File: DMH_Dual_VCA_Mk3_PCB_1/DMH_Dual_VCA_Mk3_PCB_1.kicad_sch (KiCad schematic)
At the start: 0 parts

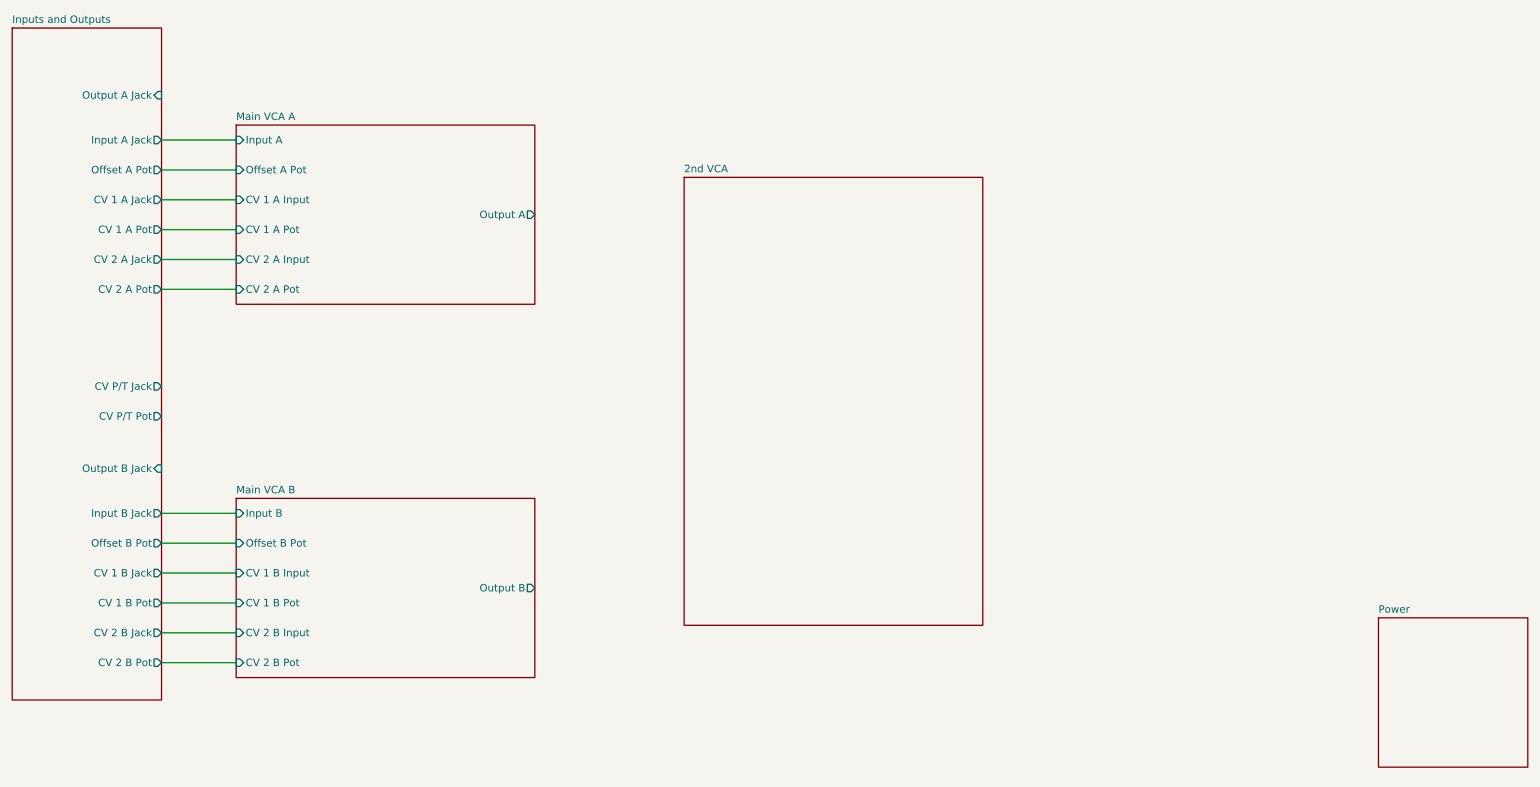
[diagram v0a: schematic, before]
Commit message: 2nd VCA design done
Clipping design in progress
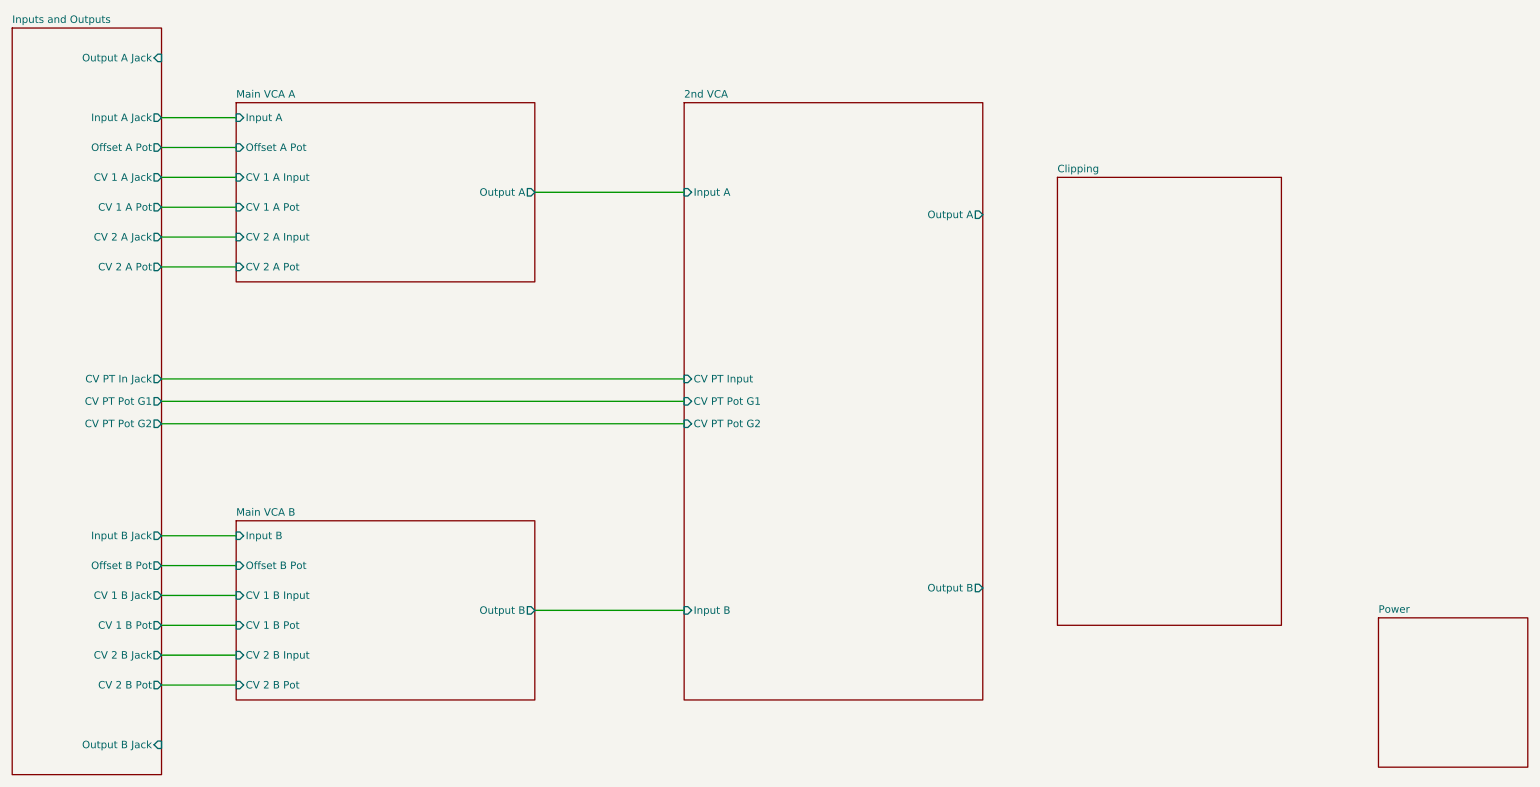
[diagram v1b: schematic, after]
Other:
- added sheet Clipping (Clipping.kicad_sch)
- sheet 2nd VCA ports: added CV PT Input, CV PT Pot G1, CV PT Pot G2, Input A, Input B, Output A, Output B; removed none
- sheet Inputs and Outputs ports: added CV PT In Jack, CV PT Pot G1, CV PT Pot G2; removed CV P/T Jack, CV P/T Pot

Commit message: Designed clip and dist circuit
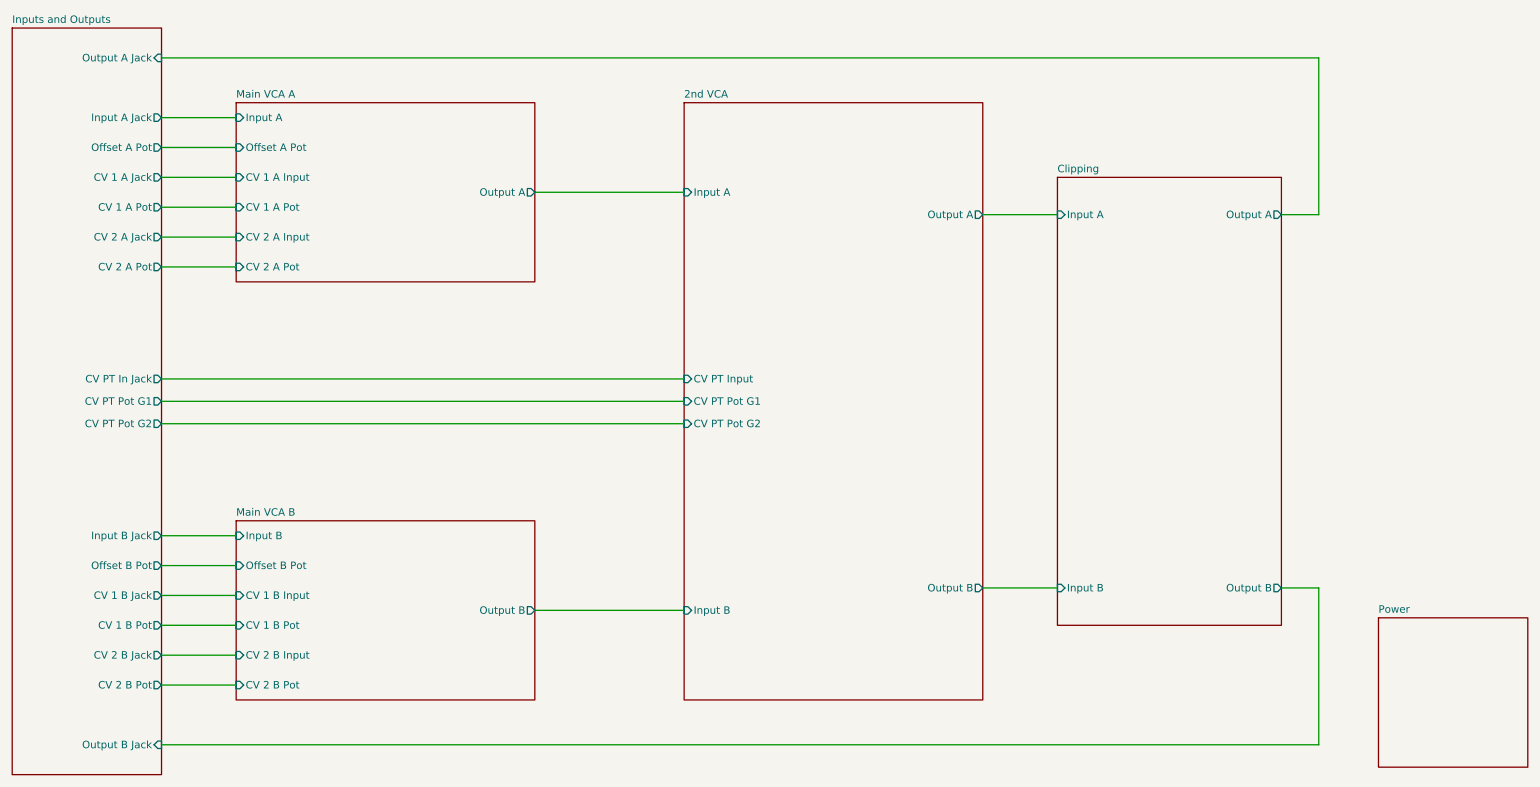
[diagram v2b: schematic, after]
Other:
- sheet Clipping ports: added Input A, Input B, Output A, Output B; removed none
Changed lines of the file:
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@@
+	(wire
+		(pts
+			(xy 247.65 69.85) (xy 247.65 43.18)
+		)
+		(stroke
+			(width 0)
+			(type default)
+		)
+	)
 	(wire
 		(pts
@@
 	(wire
 		(pts
+			(xy 247.65 43.18) (xy 50.8 43.18)
+		)
+		(stroke
+			(width 0)
+			(type default)
+		)
+	)
+	(wire
+		(pts
+			(xy 247.65 160.02) (xy 50.8 160.02)
+		)
+		(stroke
+			(width 0)
+			(type default)
+		)
+	)
+	(wire
+		(pts
+			(xy 247.65 133.35) (xy 247.65 160.02)
+		)
+		(stroke
+			(width 0)
+			(type default)
+		)
+	)
+	(wire
+		(pts
+			(xy 241.3 133.35) (xy 247.65 133.35)
+		)
+		(stroke
+			(width 0)
+			(type default)
+		)
+	)
+	(wire
+		(pts
 			(xy 50.8 101.6) (xy 139.7 101.6)
 		)
@@
 	(wire
 		(pts
+			(xy 190.5 69.85) (xy 203.2 69.85)
+		)
+		(stroke
+			(width 0)
+			(type default)
+		)
+	)
+	(wire
+		(pts
 			(xy 50.8 134.62) (xy 63.5 134.62)
 		)
@@
 		(pts
 			(xy 50.8 68.58) (xy 63.5 68.58)
+		)
+		(stroke
+			(width 0)
+			(type default)
+		)
+	)
+	(wire
+		(pts
+			(xy 190.5 133.35) (xy 203.2 133.35)
+		)
+		(stroke
+			(width 0)
+			(type default)
+		)
+	)
+	(wire
+		(pts
+			(xy 241.3 69.85) (xy 247.65 69.85)
 		)
 		(stroke
@@
 			)
 		)
+		(pin "Input A" input
+			(at 203.2 69.85 180)
+			(effects
+				(font
+					(size 1.27 1.27)
+				)
+				(justify left)
+			)
+		)
+		(pin "Input B" input
+			(at 203.2 133.35 180)
+			(effects
+				(font
+					(size 1.27 1.27)
+				)
+				(justify left)
+			)
+		)
+		(pin "Output A" output
+			(at 241.3 69.85 0)
+			(effects
+				(font
+					(size 1.27 1.27)
+				)
+				(justify right)
+			)
+		)
+		(pin "Output B" output
+			(at 241.3 133.35 0)
+			(effects
+				(font
+					(size 1.27 1.27)
+				)
+				(justify right)
+			)
+		)

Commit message: Synced PCB 1 and 2 schematics
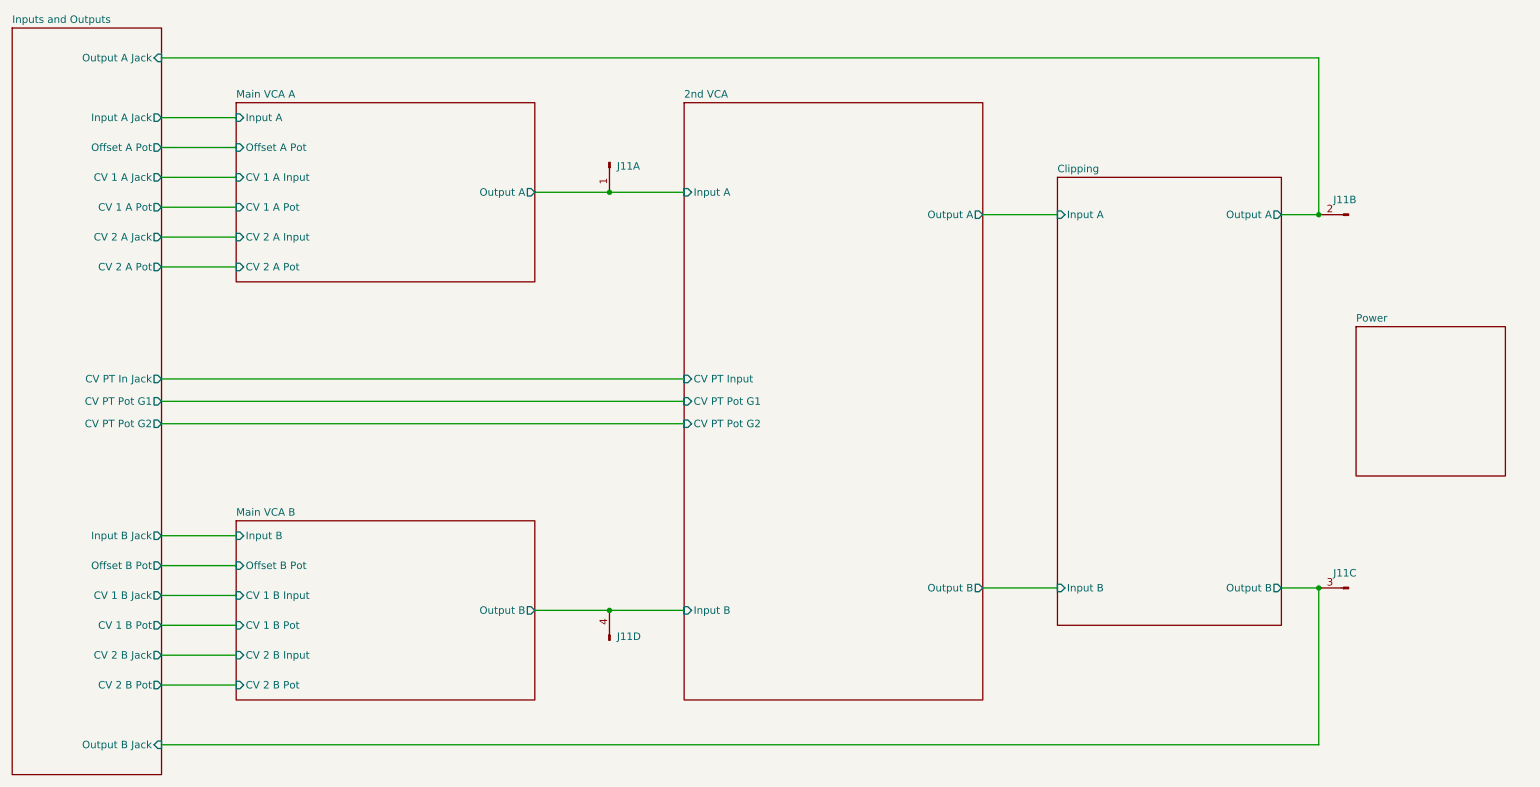
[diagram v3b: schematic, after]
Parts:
- added J11: Conn_01x04_PinHeader, Connector_PinHeader_2.54mm:PinHeader_1x04_P2.54mm_Vertical, symbol SynthStuff:Conn_01x04_PinHeader
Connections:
- net 2nd VCA/Input A: now also J11.1 (Pin_1)
- net 2nd VCA/Input B: now also J11.4 (Pin_4)
- net Clipping/Output A: now also J11.2 (Pin_2)
- net Clipping/Output B: now also J11.3 (Pin_3)
